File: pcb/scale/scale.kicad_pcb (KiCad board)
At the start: 2 copper layers, 103.8 x 47.9 mm, 89 parts, among them J1 USB_C_Receptacle_USB2.0, J2 Conn_01x07, J3 Conn_01x04, SW1 SW_Push, SW10 SW_Push, SW11 SW_Push, SW12 SW_Push, SW13 SW_Push, SW14 SW_Push, SW15 SW_Push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

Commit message: 移动电源键
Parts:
- moved D1 1.40 mm to (120.1, 86.4)
- moved R1 1.40 mm to (120.1, 83.6)
- moved R2 1.40 mm to (124.0, 92.5)
- moved R9 1.40 mm to (124.0, 89.9)
- moved SW1 1.40 mm to (122.9, 85.1)
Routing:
- net /WKUP: track 76.1 -> 74.7 mm
- net /DPWR_EN: track 45.4 -> 44.2 mm
- net +BATT: track 107.4 -> 108.0 mm
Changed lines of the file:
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@@
   )
   (footprint "Resistor_SMD:R_0402_1005Metric" (layer "F.Cu")
-    (at 125.349 92.456 -90)
+    (at 123.952 92.456 -90)
     (descr "Resistor SMD 0402 (1005 Metric), square (rectangular) end terminal, IPC_7351 nominal, (Body size source: IPC-SM-782 page 72, https://www.pcb-3d.com/wordpress/wp-content/uploads/ipc-sm-782a_amendment_1_and_2.pdf), generated with kicad-footprint-generator")
     (tags "resistor")
@@
   )
   (footprint "Diode_SMD:D_SOD-523" (layer "F.Cu")
-    (at 121.539 86.36 -90)
+    (at 120.142 86.36 -90)
     (descr "http://www.diodes.com/datasheets/ap02001.pdf p.144")
     (tags "Diode SOD523")
@@
   )
   (footprint "Resistor_SMD:R_0402_1005Metric" (layer "F.Cu")
-    (at 125.349 89.8652 -90)
+    (at 123.952 89.8652 -90)
     (descr "Resistor SMD 0402 (1005 Metric), square (rectangular) end terminal, IPC_7351 nominal, (Body size source: IPC-SM-782 page 72, https://www.pcb-3d.com/wordpress/wp-content/uploads/ipc-sm-782a_amendment_1_and_2.pdf), generated with kicad-footprint-generator")
     (tags "resistor")
@@
   )
   (footprint "Resistor_SMD:R_0402_1005Metric" (layer "F.Cu")
-    (at 121.539 83.566 90)
+    (at 120.142 83.566 90)
     (descr "Resistor SMD 0402 (1005 Metric), square (rectangular) end terminal, IPC_7351 nominal, (Body size source: IPC-SM-782 page 72, https://www.pcb-3d.com/wordpress/wp-content/uploads/ipc-sm-782a_amendment_1_and_2.pdf), generated with kicad-footprint-generator")
     (tags "resistor")
@@
   )
   (footprint "Button_Switch_SMD:SW_Push_SPST_NO_Alps_SKRK" (layer "F.Cu")
-    (at 124.333 85.09 90)
+    (at 122.936 85.09 90)
     (descr "http://www.alps.com/prod/info/E/HTML/Tact/SurfaceMount/SKRK/SKRKAHE020.html")
     (tags "SMD SMT button")
@@
   (segment (start 135.636 56.5912) (end 136.8044 55.4228) (width 0.25) (layer "F.Cu") (net 1))
   (via (at 135.636 59.3598) (size 0.8) (drill 0.4) (layers "F.Cu" "B.Cu") (net 1))
-  (via (at 124.333 82.9564) (size 0.8) (drill 0.4) (layers "F.Cu" "B.Cu") (net 1))
+  (via (at 122.936 82.9564) (size 0.8) (drill 0.4) (layers "F.Cu" "B.Cu") (net 1))
   (via (at 106.8324 63.754) (size 0.6) (drill 0.3) (layers "F.Cu" "B.Cu") (net 1))
   (via (at 136.8044 55.4228) (size 0.8) (drill 0.4) (layers "F.Cu" "B.Cu") (net 1))
@@
   (segment (start 110.6932 56.0832) (end 108.0839 56.0832) (width 0.3) (layer "B.Cu") (net 1))
   (segment (start 135.0162 55.3488) (end 136.6644 55.3488) (width 0.5) (layer "B.Cu") (net 1))
-  (segment (start 135.636 59.3598) (end 135.636 60.833) (width 0.25) (layer "B.Cu") (net 1))
   (segment (start 108.0839 56.0832) (end 108.0828 56.0821) (width 0.3) (layer "B.Cu") (net 1))
   (segment (start 106.9696 55.5854) (end 106.9696 53.34) (width 0.5) (layer "B.Cu") (net 1))
   (segment (start 145.7154 54.9938) (end 145.4154 54.6938) (width 0.5) (layer "B.Cu") (net 1))
-  (segment (start 135.636 60.833) (end 124.333 72.136) (width 0.25) (layer "B.Cu") (net 1))
   (segment (start 140.6814 52.8828) (end 121.412 52.8828) (width 0.5) (layer "B.Cu") (net 1))
   (segment (start 135.0162 55.3488) (end 135.0264 55.359) (width 0.4) (layer "B.Cu") (net 1))
-  (segment (start 124.333 72.136) (end 124.333 82.9564) (width 0.25) (layer "B.Cu") (net 1))
+  (segment (start 122.936 72.136) (end 122.936 82.9564) (width 0.25) (layer "B.Cu") (net 1))
   (segment (start 110.6932 57.7342) (end 110.6932 56.0832) (width 0.5) (layer "B.Cu") (net 1))
   (segment (start 145.923 54.9808) (end 147.9344 54.9808) (width 0.5) (layer "B.Cu") (net 1))
@@
   (segment (start 150.2209 55.1688) (end 148.2956 55.1688) (width 0.5) (layer "B.Cu") (net 1))
   (segment (start 142.4924 54.6938) (end 142.3924 54.5938) (width 0.4) (layer "B.Cu") (net 1))
+  (segment (start 122.936 72.136) (end 135.636 59.436) (width 0.25) (layer "B.Cu") (net 1))
   (segment (start 107.4663 56.0821) (end 106.9696 55.5854) (width 0.5) (layer "B.Cu") (net 1))
   (segment (start 108.8774 59.6262) (end 108.8774 58.674) (width 0.25) (layer "B.Cu") (net 1))
   (segment (start 136.6644 55.3488) (end 136.8044 55.4888) (width 0.4) (layer "B.Cu") (net 1))
   (segment (start 121.412 52.8828) (end 118.2116 56.0832) (width 0.5) (layer "B.Cu") (net 1))
+  (segment (start 135.636 59.436) (end 135.636 59.3598) (width 0.25) (layer "B.Cu") (net 1))
   (segment (start 105.5598 70.8686) (end 105.5344 70.8686) (width 0.3) (layer "F.Cu") (net 2))
   (segment (start 117.843 53.2554) (end 117.5212 52.9336) (width 0.2) (layer "F.Cu") (net 2))
@@
   (segment (start 108.839 67.3608) (end 114.3508 67.3608) (width 0.3) (layer "B.Cu") (net 5))
   (segment (start 108.8644 71.628) (end 108.8644 67.3862) (width 0.3) (layer "B.Cu") (net 5))
-  (segment (start 125.349 88.206) (end 125.349 89.3552) (width 0.25) (layer "F.Cu") (net 6))
-  (segment (start 125.349 88.206) (end 124.333 87.19) (width 0.25) (layer "F.Cu") (net 6))
-  (segment (start 121.669 87.19) (end 121.539 87.06) (width 0.25) (layer "F.Cu") (net 6))
-  (segment (start 124.333 87.19) (end 121.669 87.19) (width 0.25) (layer "F.Cu") (net 6))
+  (segment (start 123.952 88.206) (end 123.952 89.3552) (width 0.25) (layer "F.Cu") (net 6))
+  (segment (start 123.952 88.206) (end 122.936 87.19) (width 0.25) (layer "F.Cu") (net 6))
+  (segment (start 120.272 87.19) (end 120.142 87.06) (width 0.25) (layer "F.Cu") (net 6))
+  (segment (start 122.936 87.19) (end 120.272 87.19) (width 0.25) (layer "F.Cu") (net 6))
   (segment (start 151.9174 57.5564) (end 155.3718 54.102) (width 0.25) (layer "F.Cu") (net 7))
   (segment (start 163.4745 54.102) (end 155.3718 54.102) (width 0.25) (layer "F.Cu") (net 7))
@@
   (segment (start 154.2059 58.9303) (end 154.2674 58.9918) (width 0.25) (layer "B.Cu") (net 15))
   (segment (start 154.2059 57.4018) (end 154.2059 58.9303) (width 0.25) (layer "B.Cu") (net 15))
-  (segment (start 121.539 85.66) (end 121.539 84.076) (width 0.25) (layer "F.Cu") (net 16))
+  (segment (start 120.142 85.66) (end 120.142 84.076) (width 0.25) (layer "F.Cu") (net 16))
   (segment (start 110.883 65.9415) (end 110.883 60.9486) (width 0.25) (layer "F.Cu") (net 17))
   (segment (start 110.883 60.9486) (end 110.6424 60.708) (width 0.25) (layer "F.Cu") (net 17))
@@
   (segment (start 78.6155 55.1757) (end 78.978 54.8132) (width 0.25) (layer "B.Cu") (net 20))
   (segment (start 120.12785 63.9572) (end 120.12785 67.22255) (width 0.25) (layer "F.Cu") (net 21))
-  (segment (start 121.539 83.056) (end 121.539 82.296) (width 0.25) (layer "F.Cu") (net 21))
+  (segment (start 120.142 83.056) (end 120.142 82.296) (width 0.25) (layer "F.Cu") (net 21))
   (segment (start 120.12785 67.22255) (end 118.9964 68.354) (width 0.25) (layer "F.Cu") (net 21))
   (segment (start 118.9964 68.354) (end 115.7955 68.354) (width 0.25) (layer "F.Cu") (net 21))
-  (via (at 121.539 82.296) (size 0.8) (drill 0.4) (layers "F.Cu" "B.Cu") (net 21))
+  (via (at 120.142 82.296) (size 0.8) (drill 0.4) (layers "F.Cu" "B.Cu") (net 21))
   (via (at 120.12785 63.9572) (size 0.8) (drill 0.4) (layers "F.Cu" "B.Cu") (net 21))
-  (segment (start 121.539 65.36835) (end 120.12785 63.9572) (width 0.25) (layer "B.Cu") (net 21))
-  (segment (start 121.539 82.296) (end 121.539 65.36835) (width 0.25) (layer "B.Cu") (net 21))
-  (segment (start 131.4958 61.9252) (end 133.3699 60.0511) (width 0.25) (layer "B.Cu") (net 21))
+  (segment (start 122.15985 61.9252) (end 130.3528 61.9252) (width 0.25) (layer "B.Cu") (net 21))
   (segment (start 120.12785 63.9572) (end 122.15985 61.9252) (width 0.25) (layer "B.Cu") (net 21))
-  (segment (start 122.15985 61.9252) (end 131.4958 61.9252) (width 0.25) (layer "B.Cu") (net 21))
-  (segment (start 133.3699 60.0511) (end 133.3699 57.2488) (width 0.25) (layer "B.Cu") (net 21))
+  (segment (start 120.142 82.296) (end 120.142 63.97135) (width 0.25) (layer "B.Cu") (net 21))
+  (segment (start 133.3699 58.9081) (end 133.3699 57.2488) (width 0.25) (layer "B.Cu") (net 21))
+  (segment (start 120.142 63.97135) (end 120.12785 63.9572) (width 0.25) (layer "B.Cu") (net 21))
+  (segment (start 130.3528 61.9252) (end 133.3699 58.9081) (width 0.25) (layer "B.Cu") (net 21))
   (segment (start 112.383 85.0258) (end 108.4326 88.9762) (width 0.25) (layer "F.Cu") (net 22))
   (segment (start 112.383 74.2665) (end 112.383 85.0258) (width 0.25) (layer "F.Cu") (net 22))
+  (segment (start 90.424 93.726) (end 120.6012 93.726) (width 0.25) (layer "F.Cu") (net 24))
   (segment (start 106.0196 72.4408) (end 106.0196 74.0664) (width 0.2) (layer "F.Cu") (net 24))
   (segment (start 106.0196 74.0664) (end 98.806 81.28) (width 0.25) (layer "F.Cu") (net 24))
   (segment (start 88.9 81.28) (end 86.868 83.312) (width 0.25) (layer "F.Cu") (net 24))
-  (segment (start 125.349 90.3752) (end 125.349 91.946) (width 0.25) (layer "F.Cu") (net 24))
+  (segment (start 123.952 90.3752) (end 123.952 91.946) (width 0.25) (layer "F.Cu") (net 24))
   (segment (start 86.868 83.312) (end 86.868 90.17) (width 0.25) (layer "F.Cu") (net 24))
-  (segment (start 90.424 93.726) (end 121.9982 93.726) (width 0.25) (layer "F.Cu") (net 24))
   (segment (start 98.806 81.28) (end 88.9 81.28) (width 0.25) (layer "F.Cu") (net 24))
   (segment (start 86.868 90.17) (end 90.424 93.726) (width 0.25) (layer "F.Cu") (net 24))
-  (segment (start 121.9982 93.726) (end 125.349 90.3752) (width 0.25) (layer "F.Cu") (net 24))
+  (segment (start 120.6012 93.726) (end 123.952 90.3752) (width 0.25) (layer "F.Cu") (net 24))
   (segment (start 106.6064 71.854) (end 106.0196 72.4408) (width 0.2) (layer "F.Cu") (net 24))
   (segment (start 107.4705 71.854) (end 106.6064 71.854) (width 0.2) (layer "F.Cu") (net 24))

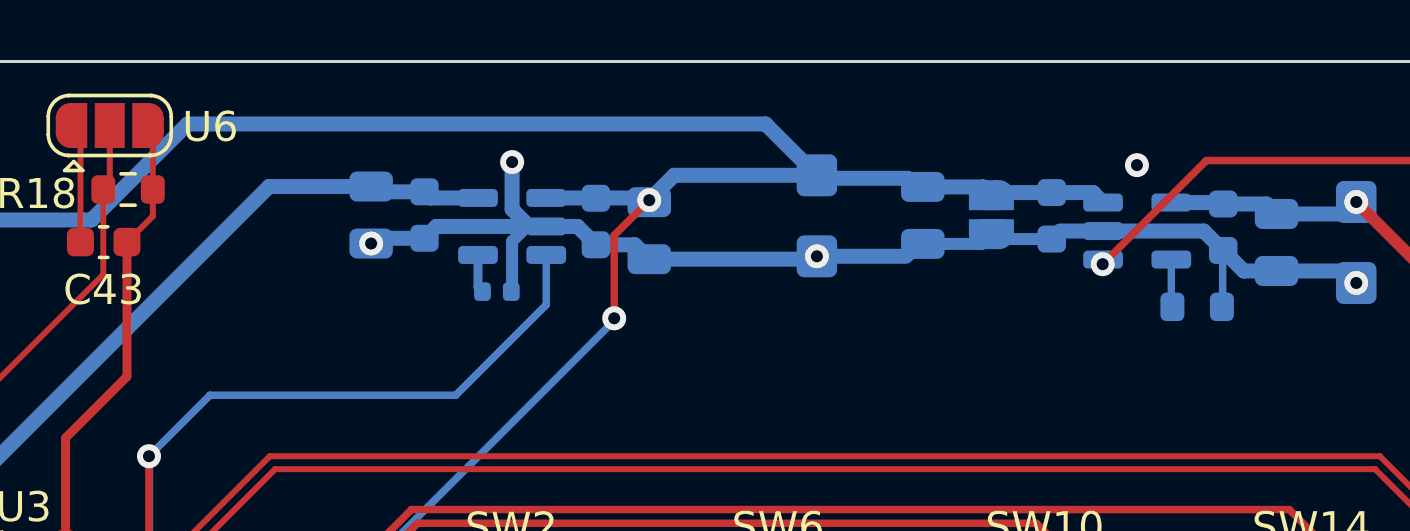
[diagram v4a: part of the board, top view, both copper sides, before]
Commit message: 清空电池接线附近和加粗TP4065 PROG线
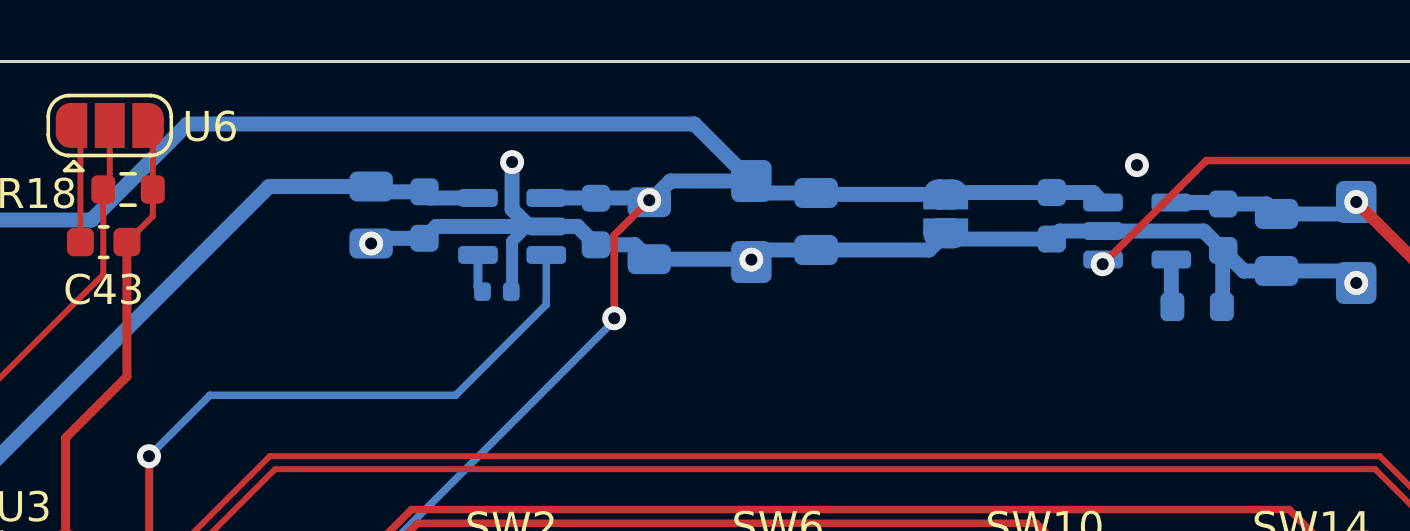
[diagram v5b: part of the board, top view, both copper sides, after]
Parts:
- moved C4 3.56 mm to (142.4, 56.1)
- moved C15 2.19 mm to (140.2, 56.1)
- moved BT1 1.52 mm to (146.7, 55.9)
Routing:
- net +BATT: track 108.0 -> 106.0 mm

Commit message: 添加电池正极标志
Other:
- board text added: "+"
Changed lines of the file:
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@@
     (effects (font (size 1 1) (thickness 0.15)) (justify left mirror))
+  )
+  (gr_text "+" (at 145.288 54.102) (layer "B.SilkS")
+    (effects (font (size 1.2 1.2) (thickness 0.2)) (justify mirror))
   )
   (gr_text "E+\nS-\nS+\nE-" (at 77.978 55.626 90) (layer "F.SilkS")

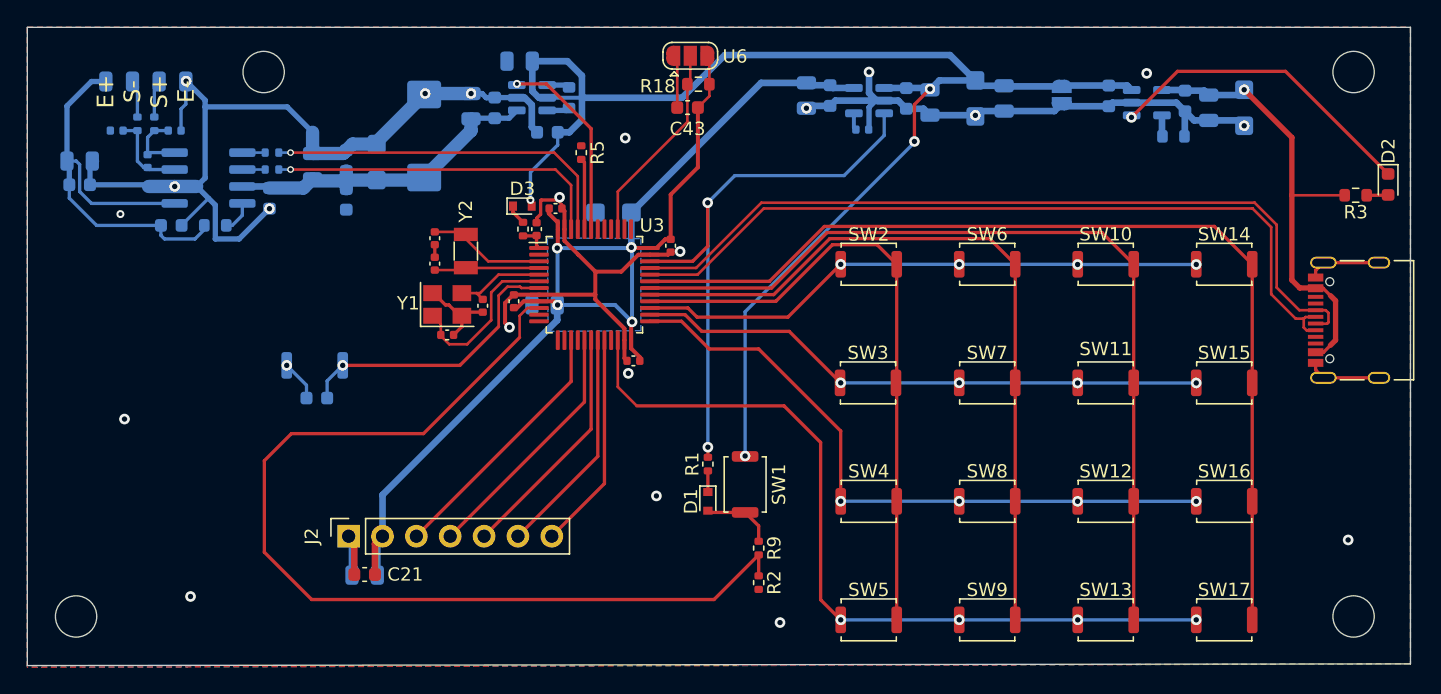
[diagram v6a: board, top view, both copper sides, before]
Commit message: PCB宽度缩小到100mm
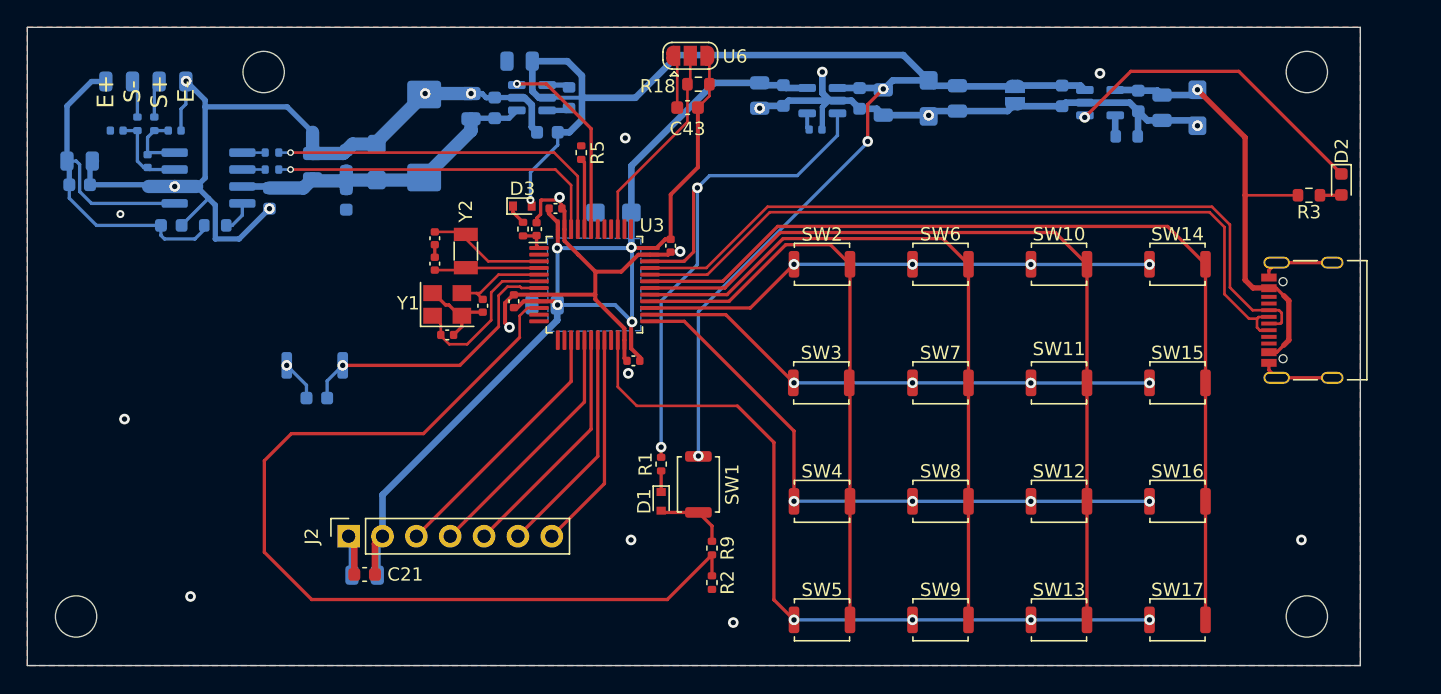
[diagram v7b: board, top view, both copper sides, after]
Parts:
- moved BT1 3.51 mm to (143.2, 55.9)
- moved C1 3.51 mm to (156.9, 56.8)
- moved C15 3.51 mm to (136.7, 56.1)
- moved C2 3.51 mm to (154.2, 56.8)
- moved C26 3.51 mm to (128.2, 58.5)
- moved C3 3.51 mm to (146.7, 55.9)
- moved C6 3.51 mm to (152.4, 56.3)
- moved C7 3.51 mm to (131.5, 56.1)
- moved D2 3.51 mm to (167.7, 62.6)
- moved J1 3.51 mm to (164.7, 72.8)
- moved R3 3.51 mm to (165.2, 63.4)
- moved R4 3.51 mm to (151.6, 59.0)
- moved SW1 3.51 mm to (119.4, 85.1)
- moved SW10 3.51 mm to (146.5, 68.6)
- moved SW11 3.51 mm to (146.5, 77.5)
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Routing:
- net /KB_Row1: track 42.9 -> 38.8 mm
- net /UD+: track 60.8 -> 57.1 mm
- net /UD-: track 60.1 -> 56.3 mm
- net /KB_Row3: track 49.7 -> 46.2 mm
- net /KB_Col4: track 74.7 -> 71.2 mm
- net /KB_Col2: track 56.6 -> 53.1 mm
- net /WKUP: track 74.7 -> 71.2 mm
- net +BATT: track 106.0 -> 102.5 mm
- net /KB_Row4: track 61.1 -> 57.5 mm
- net /KB_Col3: track 65.7 -> 62.2 mm
- net /KB_Col1: track 47.6 -> 44.0 mm
- net /KB_Row2: track 43.1 -> 39.6 mm
- net +3V3: track 102.9 -> 101.5 mm
- net /DPWR_EN: track 44.2 -> 43.6 mm
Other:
- board size 103.8 x 47.9 mm -> 100 x 47.9 mm
